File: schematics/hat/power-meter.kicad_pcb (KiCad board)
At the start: 2 copper layers, 65 x 56.5 mm, 113 parts, among them J1 EEPROM WE, J2 40HAT, P1 3mm mounting hole, P10 INPUT 5, P11 INPUT 6, P12 INPUT 7, P13 OSHW LOGO, P14 KICAD LOGO, P15 JC128, P16 JC128, P17 JC128, P18 JC128, P19 JC128, P2 3mm mounting hole, P20 JC128, P21 JC128, P22 JC128, P3 3mm mounting hole, P4 3mm mounting hole, P5 INPUT 0, P6 INPUT 1, P7 INPUT 2, P8 INPUT 3, P9 INPUT 4, U1 CAT24C32, U2 MCP3008

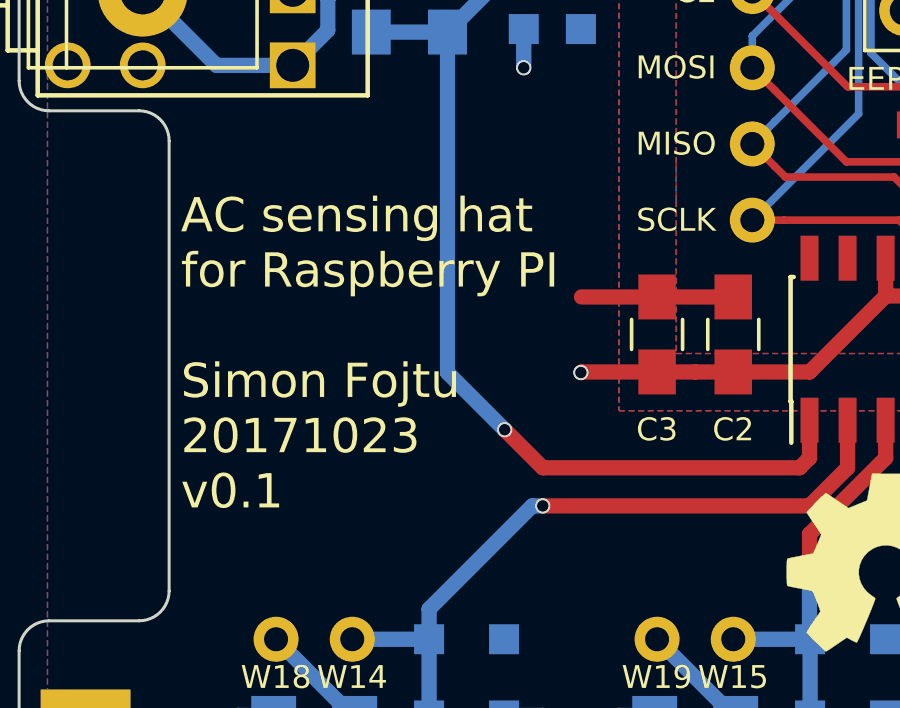
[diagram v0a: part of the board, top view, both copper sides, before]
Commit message: 3F voltage frontend: add logo, revision, renaming a moving
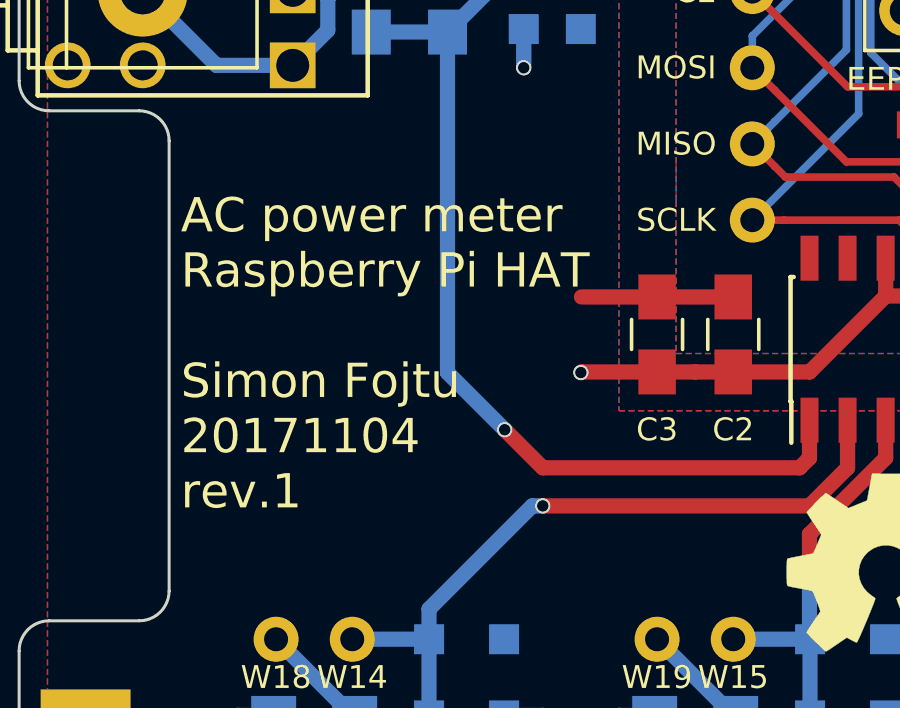
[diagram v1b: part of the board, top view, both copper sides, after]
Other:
- board text added: "AC power meter Raspberry Pi HAT Simon Fojtu 20171104 rev.1"
- board text removed: "AC sensing hat for Raspberry PI Simon Fojtu 20171023 v0.1"
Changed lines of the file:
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@@
   (general
     (links 198)
-    (no_connects 18)
-    (area 66.949999 56.949999 132.050001 113.550001)
+    (no_connects 0)
+    (area 64.392599 55.88 134.997401 116.582401)
     (thickness 1.6)
     (drawings 24)
@@
   )
   (page A4)
+  (title_block
+    (title "AC power meter Raspberry Pi HAT")
+    (date 2017-11-04)
+    (rev 1)
+    (company "Simon Fojtu")
+  )
   (layers
     (0 F.Cu signal)
@@
   )
   (setup
-    (last_trace_width 0.508)
+    (last_trace_width 0.254)
     (user_trace_width 0.1524)
     (user_trace_width 0.254)
@@
     (pcbplotparams
       (layerselection 0x010f0_80000001)
-      (usegerberextensions false)
+      (usegerberextensions true)
       (excludeedgelayer true)
       (linewidth 0.100000)
@@
     (effects (font (size 0.762 0.762) (thickness 0.127)))
   )
-  (gr_text "AC sensing hat\nfor Raspberry PI\n\nSimon Fojtu\n20171023\nv0.1" (at 72.39 85.09) (layer F.SilkS)
+  (gr_text "AC power meter\nRaspberry Pi HAT\n\nSimon Fojtu\n20171104\nrev.1" (at 72.39 85.09) (layer F.SilkS)
     (effects (font (size 1.143 1.143) (thickness 0.2032)) (justify left))
   )
